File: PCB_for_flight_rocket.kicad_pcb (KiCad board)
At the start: 2 copper layers, 100 x 100 mm, 20 parts, among them U1 MC34063AP, U2 LM1117T-3.3, U4 A000005

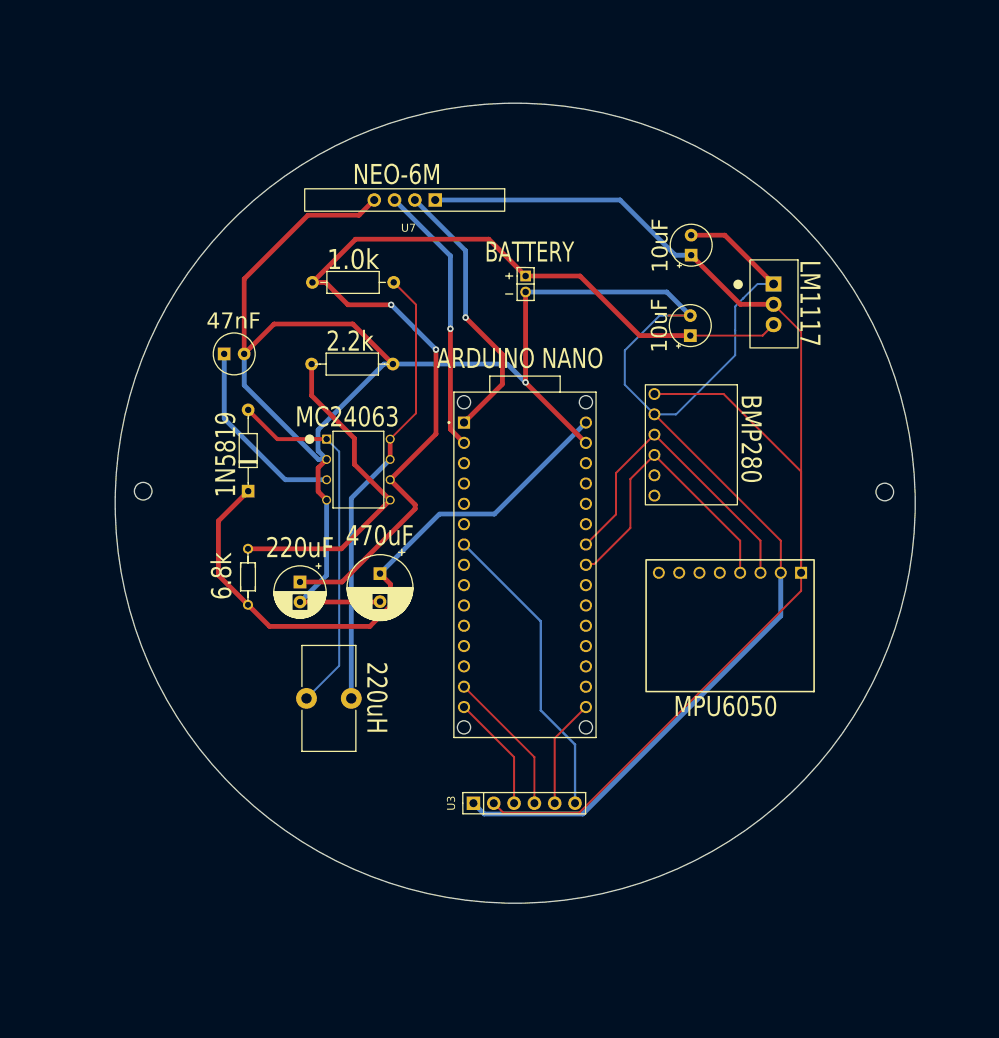
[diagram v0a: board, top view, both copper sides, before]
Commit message: Added ground plane
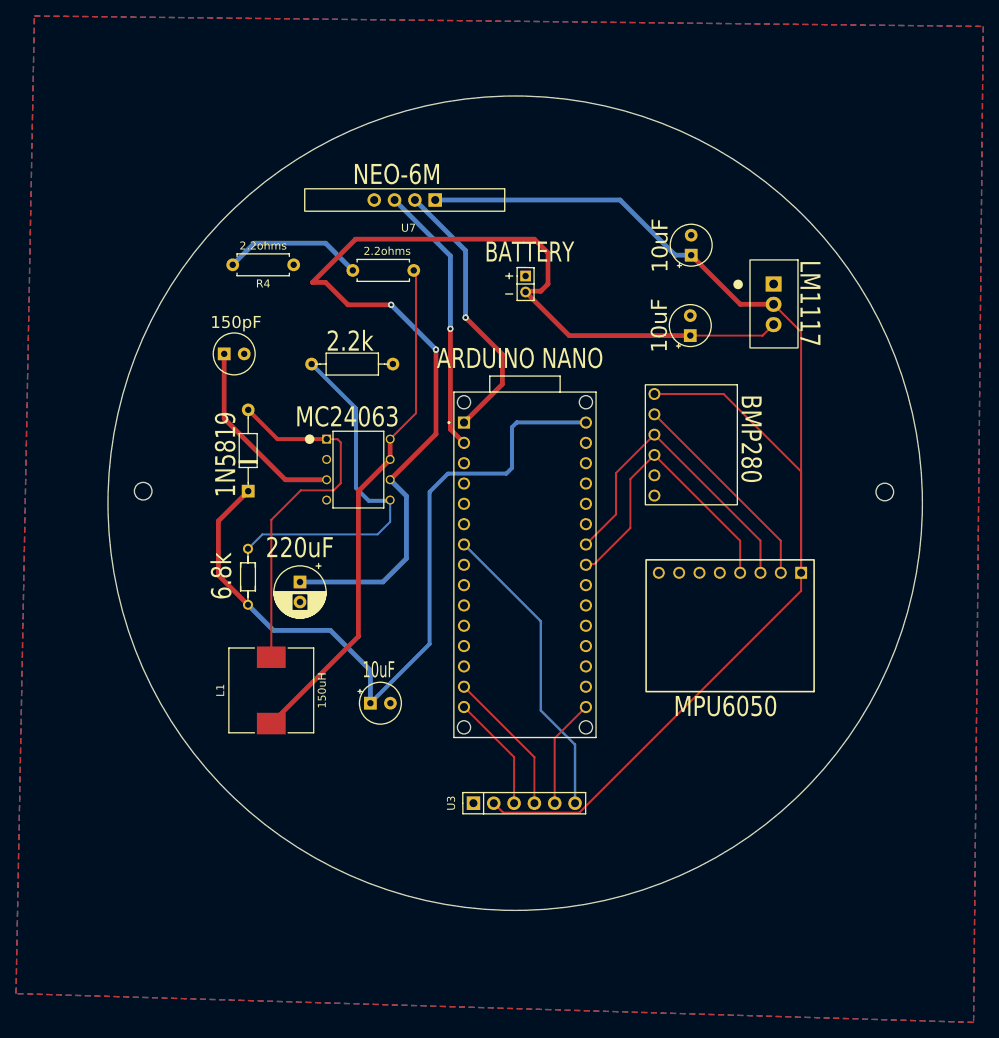
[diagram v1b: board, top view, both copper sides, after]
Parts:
- added R4: 2.2ohms, Resistor_THT:R_Axial_DIN0207_L6.3mm_D2.5mm_P7.62mm_Horizontal, F.Cu at (80.8, 71.1)
- C4: value 47nF -> 150pF
- C5: value 470uF -> 10uF; footprint lib:Capacitor_470uF -> lib:capacitor_10uF
- L1: value 220uH 5A -> 150uH; footprint lib:inductor_220uH -> Inductor_SMD:L_10.4x10.4_H4.8
- R1: value 1 -> 2.2ohms; footprint lib:resistor_1k -> Resistor_THT:R_Axial_DIN0207_L6.3mm_D2.5mm_P7.62mm_Horizontal
- moved C5 19.9 mm to (92.4, 130.9), turned to 0 degrees
- turned L1 to 90 degrees
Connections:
- BT1 pad 1: +3.7V -> GND
- BT1 pad 2: GND_5V -> +3.7V
- C1 pad 2: GND_5V -> GND
- C4 pad 2: GND_5V -> GND
- C5 pad 2: GND_5V -> GND
- R1 pad 1: +3.7V -> Net-(R1-Pad1)
- R3 pad 2: GND_5V -> GND
- U1 pad 2: GND_5V -> GND
- U1 pad 4: GND_5V -> GND
- U4 pad 29: GND_5V -> GND
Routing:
- net GND: track 215.0 -> 26.4 mm
- net GND_5V: track 104.6 -> 0.00 mm, vias 1 -> 0
- net 5V: track 75.4 -> 95.7 mm
- net Net-(R1-Pad1): track 0.00 -> 17.5 mm
- net +3.7V: track 126.1 -> 136.1 mm
- net Net-(U1-DRVR_C): track 56.5 -> 64.3 mm
- net Net-(U1-COMPARATOR_NEG): track 41.4 -> 44.6 mm
- added copper zone on B.Cu, net GND
- added copper zone on F.Cu, net GND
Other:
- board size 100 x 100 mm -> 101.8 x 101.8 mm
